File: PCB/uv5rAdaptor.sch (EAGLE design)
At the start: 2 parts

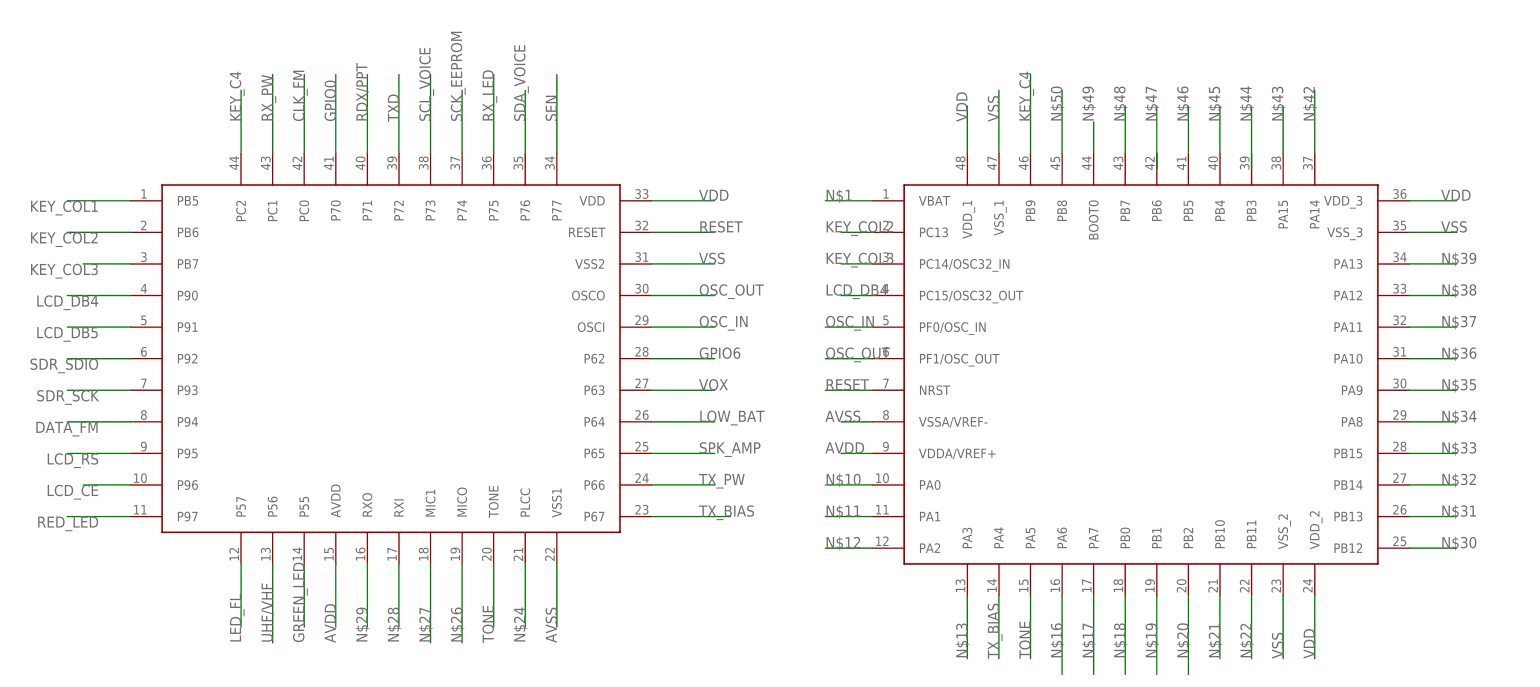
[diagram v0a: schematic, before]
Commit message: Link all points except for gpio6, we will do that once everything is routed
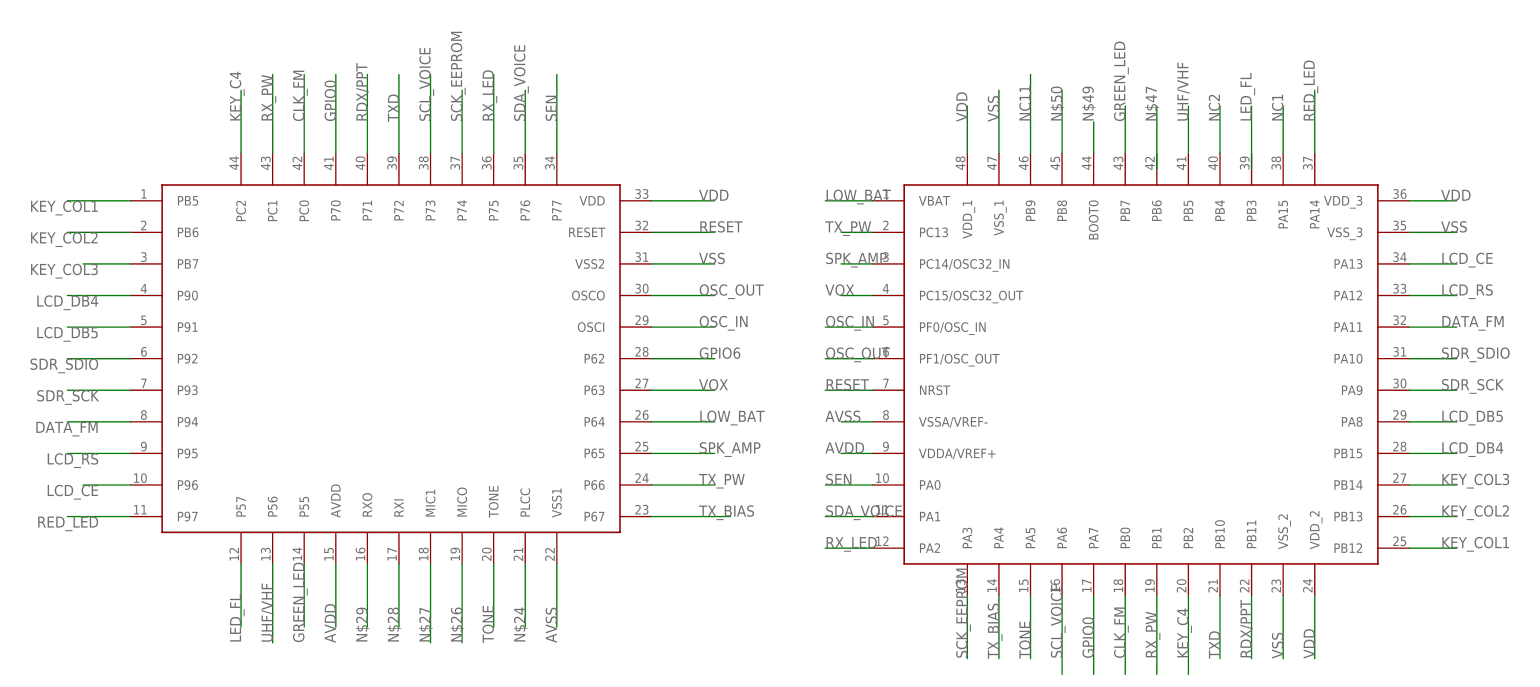
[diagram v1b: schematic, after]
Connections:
- net N$43 renamed NC1
- net N$45 renamed NC2
- removed net N$1: U$1.VBAT
- removed net N$10: U$1.PA0
- removed net N$11: U$1.PA1
- removed net N$12: U$1.PA2
- removed net N$13: U$1.PA3
- removed net N$16: U$1.PA6
- removed net N$17: U$1.PA7
- removed net N$18: U$1.PB0
- removed net N$19: U$1.PB1
- removed net N$20: U$1.PB2
- removed net N$21: U$1.PB10
- removed net N$22: U$1.PB11
- removed net N$30: U$1.PB12
- removed net N$31: U$1.PB13
- removed net N$32: U$1.PB14
- removed net N$33: U$1.PB15
- removed net N$34: U$1.PA8
- removed net N$35: U$1.PA9
- removed net N$36: U$1.PA10
- removed net N$37: U$1.PA11
- removed net N$38: U$1.PA12
- removed net N$39: U$1.PA13
- removed net N$42: U$1.PA14
- removed net N$46: U$1.PB5
- removed net N$48: U$1.PB7
- new net NC11: U$1.PB9
- net CLK_FM: now also U$1.PB0
- net DATA_FM: now also U$1.PA11
- net GPIO0: now also U$1.PA7
- net GREEN_LED: now also U$1.PB7
- net KEY_C4: now also U$1.PB2; no longer U$1.PB9
- net KEY_COL1: now also U$1.PB12
- net KEY_COL2: now also U$1.PB13; no longer U$1.PC13
- net KEY_COL3: now also U$1.PB14; no longer U$1.PC14/OSC32_IN
- net LCD_CE: now also U$1.PA13
- net LCD_DB4: now also U$1.PB15; no longer U$1.PC15/OSC32_OUT
- net LCD_DB5: now also U$1.PA8
- net LCD_RS: now also U$1.PA12
- net LOW_BAT: now also U$1.VBAT
- net RDX/PPT: now also U$1.PB11
- net RED_LED: now also U$1.PA14
- net RX_LED: now also U$1.PA2
- net RX_PW: now also U$1.PB1
- net SCK_EEPROM: now also U$1.PA3
- net SCL_VOICE: now also U$1.PA6
- net SDA_VOICE: now also U$1.PA1
- net SDR_SCK: now also U$1.PA9
- net SDR_SDIO: now also U$1.PA10
- net SEN: now also U$1.PA0
- net SPK_AMP: now also U$1.PC14/OSC32_IN
- net TXD: now also U$1.PB10
- net TX_PW: now also U$1.PC13
- net UHF/VHF: now also U$1.PB5
- net VOX: now also U$1.PC15/OSC32_OUT

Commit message: More routing
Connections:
- removed net N$50: U$1.PB8
- removed net NC1: U$1.PA15
- removed net NC11: U$1.PB9
- new net NC3: U$1.PC13
- new net NC4: U$1.PC14/OSC32_IN
- net LED_FL: now also U$1.PA15
- net SPK_AMP: now also U$1.PB9; no longer U$1.PC14/OSC32_IN
- net TX_PW: now also U$1.PB8; no longer U$1.PC13

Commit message: More traces
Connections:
- net KEY_C4: now also U$1.PB1; no longer U$1.PB2
- net RX_PW: now also U$1.PB2; no longer U$1.PB1
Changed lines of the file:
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@@
 </segment>
 <segment>
-<pinref part="U$1" gate="G$1" pin="PB2"/>
-<wire x1="142.24" y1="2.54" x2="142.24" y2="-10.16" width="0.1524" layer="91"/>
-<label x="142.24" y="-7.62" size="1.778" layer="95" rot="R90"/>
+<pinref part="U$1" gate="G$1" pin="PB1"/>
+<wire x1="137.16" y1="2.54" x2="137.16" y2="-10.16" width="0.1524" layer="91"/>
+<label x="137.16" y="-7.62" size="1.778" layer="95" rot="R90"/>
 </segment>
 </net>
@@
 </segment>
 <segment>
-<pinref part="U$1" gate="G$1" pin="PB1"/>
-<wire x1="137.16" y1="2.54" x2="137.16" y2="-10.16" width="0.1524" layer="91"/>
-<label x="137.16" y="-7.62" size="1.778" layer="95" rot="R90"/>
+<pinref part="U$1" gate="G$1" pin="PB2"/>
+<wire x1="142.24" y1="2.54" x2="142.24" y2="-10.16" width="0.1524" layer="91"/>
+<label x="142.24" y="-7.62" size="1.778" layer="95" rot="R90"/>
 </segment>
 </net>

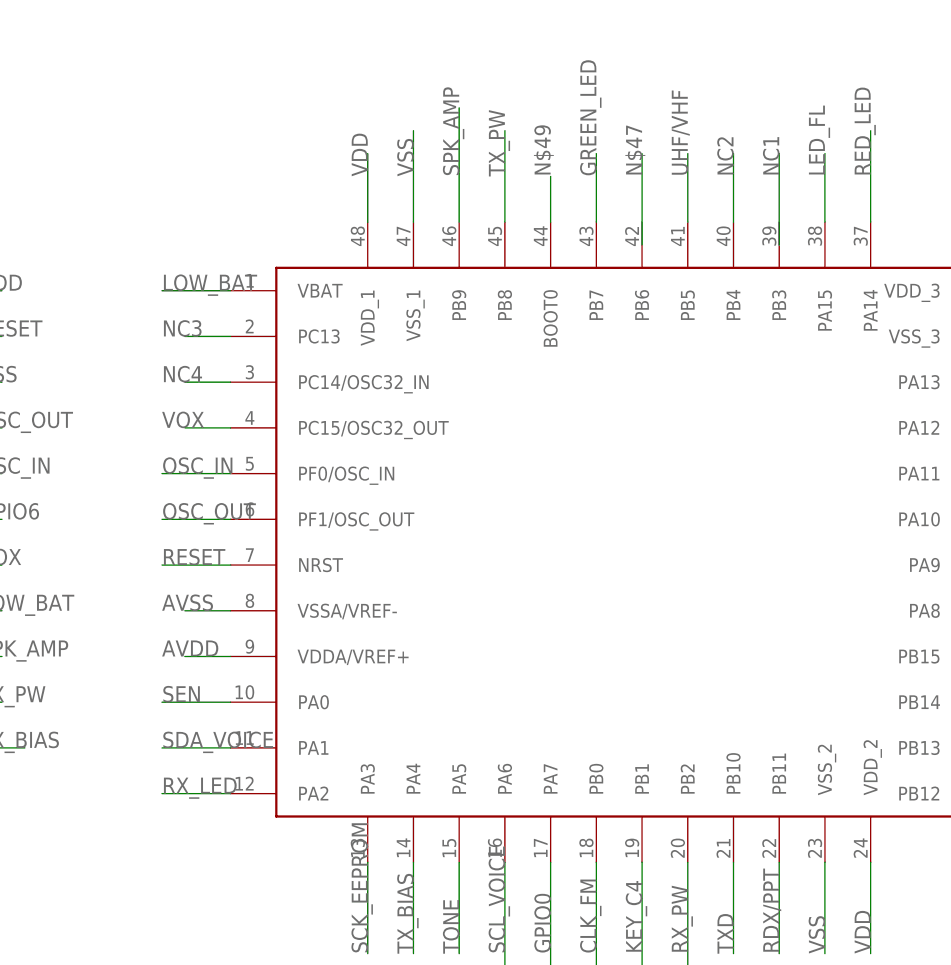
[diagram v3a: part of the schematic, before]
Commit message: Finished Routing
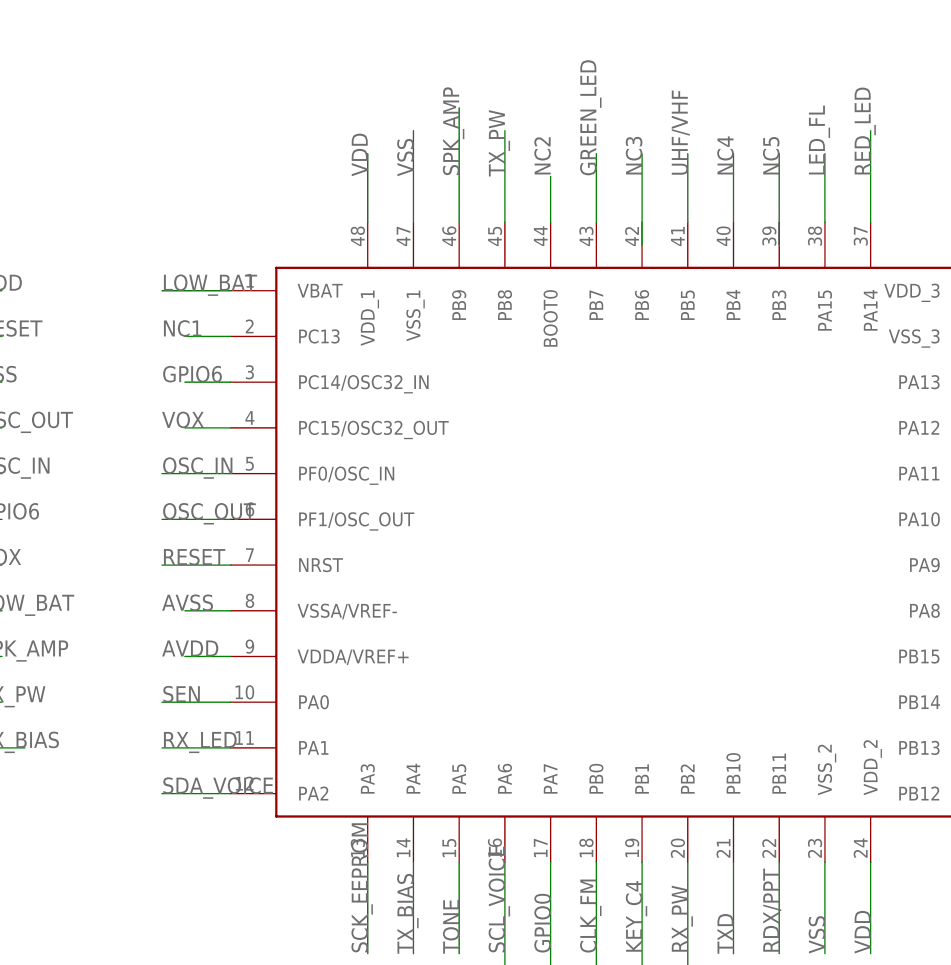
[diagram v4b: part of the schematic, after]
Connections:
- net NC3 renamed NC1
- removed net N$49: U$1.BOOT0
- net GPIO6: now also U$1.PC14/OSC32_IN
- net NC2: now also U$1.BOOT0; no longer U$1.PB4
- net NC4: now also U$1.PB4; no longer U$1.PC14/OSC32_IN
- net RX_LED: now also U$1.PA1; no longer U$1.PA2
- net SDA_VOICE: now also U$1.PA2; no longer U$1.PA1
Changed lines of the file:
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@@
+</segment>
+<segment>
+<pinref part="U$1" gate="G$1" pin="PA1"/>
+<wire x1="91.44" y1="15.24" x2="83.82" y2="15.24" width="0.1524" layer="91"/>
+<label x="83.82" y="15.24" size="1.778" layer="95"/>
+</segment>
+</net>
+<net name="SDA_VOICE" class="0">
+<segment>
+<wire x1="35.56" y1="73.66" x2="35.56" y2="83.82" width="0.1524" layer="91"/>
+<label x="35.56" y="78.74" size="1.778" layer="95" rot="R90"/>
+<pinref part="U$2" gate="G$1" pin="P76"/>
 </segment>
 <segment>
@@
 </segment>
 </net>
-<net name="SDA_VOICE" class="0">
-<segment>
-<wire x1="35.56" y1="73.66" x2="35.56" y2="83.82" width="0.1524" layer="91"/>
-<label x="35.56" y="78.74" size="1.778" layer="95" rot="R90"/>
-<pinref part="U$2" gate="G$1" pin="P76"/>
-</segment>
-<segment>
-<pinref part="U$1" gate="G$1" pin="PA1"/>
-<wire x1="91.44" y1="15.24" x2="83.82" y2="15.24" width="0.1524" layer="91"/>
-<label x="83.82" y="15.24" size="1.778" layer="95"/>
-</segment>
-</net>
 <net name="SEN" class="0">
 <segment>
@@
 <pinref part="U$2" gate="G$1" pin="P62"/>
 </segment>
+<segment>
+<pinref part="U$1" gate="G$1" pin="PC14/OSC32_IN"/>
+<wire x1="91.44" y1="55.88" x2="86.36" y2="55.88" width="0.1524" layer="91"/>
+<label x="83.82" y="55.88" size="1.778" layer="95"/>
+</segment>
 </net>
 <net name="VOX" class="0">
@@
 </segment>
 </net>
-<net name="N$47" class="0">
-<segment>
-<wire x1="137.16" y1="71.12" x2="137.16" y2="81.28" width="0.1524" layer="91"/>
-<label x="137.16" y="78.74" size="1.778" layer="95" rot="R90"/>
-</segment>
-</net>
-<net name="N$49" class="0">
+<net name="AVDD" class="0">
+<segment>
+<wire x1="5.08" y1="7.62" x2="5.08" y2="-2.54" width="0.1524" layer="91"/>
+<label x="5.08" y="-5.08" size="1.778" layer="95" rot="R90"/>
+<pinref part="U$2" gate="G$1" pin="AVDD"/>
+</segment>
+<segment>
+<pinref part="U$1" gate="G$1" pin="VDDA/VREF+"/>
+<wire x1="91.44" y1="25.4" x2="86.36" y2="25.4" width="0.1524" layer="91"/>
+<label x="83.82" y="25.4" size="1.778" layer="95"/>
+</segment>
+</net>
+<net name="AVSS" class="0">
+<segment>
+<wire x1="40.64" y1="7.62" x2="40.64" y2="-2.54" width="0.1524" layer="91"/>
+<label x="40.64" y="-5.08" size="1.778" layer="95" rot="R90"/>
+<pinref part="U$2" gate="G$1" pin="VSS1"/>
+</segment>
+<segment>
+<pinref part="U$1" gate="G$1" pin="VSSA/VREF-"/>
+<wire x1="91.44" y1="30.48" x2="86.36" y2="30.48" width="0.1524" layer="91"/>
+<label x="83.82" y="30.48" size="1.778" layer="95"/>
+</segment>
+</net>
+<net name="NC1" class="0">
+<segment>
+<pinref part="U$1" gate="G$1" pin="PC13"/>
+<wire x1="91.44" y1="60.96" x2="86.36" y2="60.96" width="0.1524" layer="91"/>
+<label x="83.82" y="60.96" size="1.778" layer="95"/>
+</segment>
+</net>
+<net name="NC2" class="0">
 <segment>
 <pinref part="U$1" gate="G$1" pin="BOOT0"/>
@@
 </segment>
 </net>
-<net name="AVDD" class="0">
-<segment>
-<wire x1="5.08" y1="7.62" x2="5.08" y2="-2.54" width="0.1524" layer="91"/>
-<label x="5.08" y="-5.08" size="1.778" layer="95" rot="R90"/>
-<pinref part="U$2" gate="G$1" pin="AVDD"/>
-</segment>
-<segment>
-<pinref part="U$1" gate="G$1" pin="VDDA/VREF+"/>
-<wire x1="91.44" y1="25.4" x2="86.36" y2="25.4" width="0.1524" layer="91"/>
-<label x="83.82" y="25.4" size="1.778" layer="95"/>
-</segment>
-</net>
-<net name="AVSS" class="0">
-<segment>
-<wire x1="40.64" y1="7.62" x2="40.64" y2="-2.54" width="0.1524" layer="91"/>
-<label x="40.64" y="-5.08" size="1.778" layer="95" rot="R90"/>
-<pinref part="U$2" gate="G$1" pin="VSS1"/>
-</segment>
-<segment>
-<pinref part="U$1" gate="G$1" pin="VSSA/VREF-"/>
-<wire x1="91.44" y1="30.48" x2="86.36" y2="30.48" width="0.1524" layer="91"/>
-<label x="83.82" y="30.48" size="1.778" layer="95"/>
-</segment>
-</net>
-<net name="NC2" class="0">
+<net name="NC3" class="0">
+<segment>
+<wire x1="137.16" y1="71.12" x2="137.16" y2="81.28" width="0.1524" layer="91"/>
+<label x="137.16" y="78.74" size="1.778" layer="95" rot="R90"/>
+</segment>
+</net>
+<net name="NC4" class="0">
 <segment>
 <pinref part="U$1" gate="G$1" pin="PB4"/>
@@
 </segment>
 </net>
-<net name="NC1" class="0">
+<net name="NC5" class="0">
 <segment>
 <wire x1="152.4" y1="71.12" x2="152.4" y2="81.28" width="0.1524" layer="91"/>
@@
 </segment>
 </net>
-<net name="NC4" class="0">
-<segment>
-<pinref part="U$1" gate="G$1" pin="PC14/OSC32_IN"/>
-<wire x1="91.44" y1="55.88" x2="86.36" y2="55.88" width="0.1524" layer="91"/>
-<label x="83.82" y="55.88" size="1.778" layer="95"/>
-</segment>
-</net>
-<net name="NC3" class="0">
-<segment>
-<pinref part="U$1" gate="G$1" pin="PC13"/>
-<wire x1="91.44" y1="60.96" x2="86.36" y2="60.96" width="0.1524" layer="91"/>
-<label x="83.82" y="60.96" size="1.778" layer="95"/>
-</segment>
-</net>

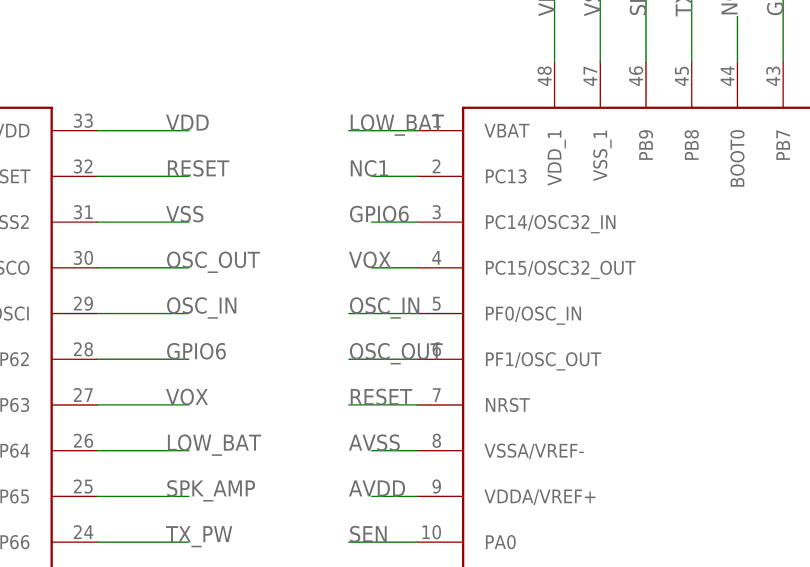
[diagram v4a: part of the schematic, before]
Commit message: Changed OSC pins to OSC32
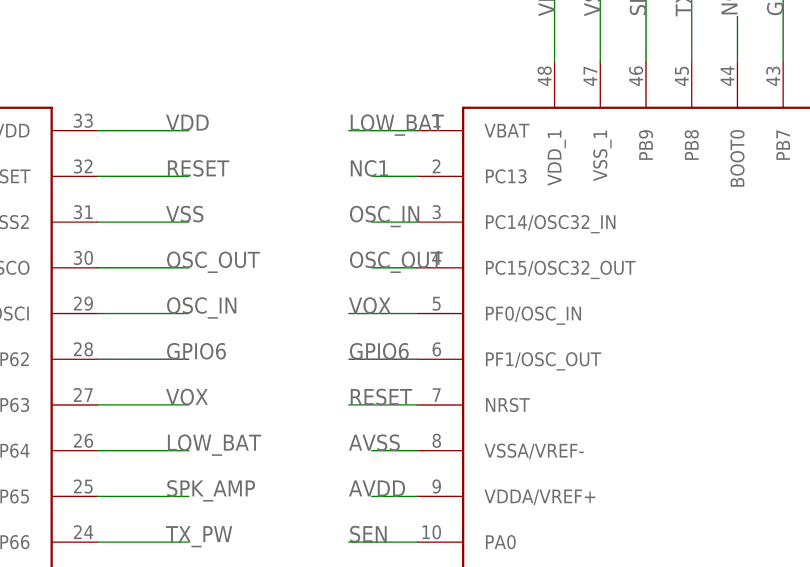
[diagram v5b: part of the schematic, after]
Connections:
- net GPIO6: now also U$1.PF1/OSC_OUT; no longer U$1.PC14/OSC32_IN
- net OSC_IN: now also U$1.PC14/OSC32_IN; no longer U$1.PF0/OSC_IN
- net OSC_OUT: now also U$1.PC15/OSC32_OUT; no longer U$1.PF1/OSC_OUT
- net VOX: now also U$1.PF0/OSC_IN; no longer U$1.PC15/OSC32_OUT
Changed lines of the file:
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@@
 </segment>
 <segment>
-<pinref part="U$1" gate="G$1" pin="PF1/OSC_OUT"/>
-<wire x1="91.44" y1="40.64" x2="83.82" y2="40.64" width="0.1524" layer="91"/>
-<label x="83.82" y="40.64" size="1.778" layer="95"/>
+<pinref part="U$1" gate="G$1" pin="PC15/OSC32_OUT"/>
+<wire x1="91.44" y1="50.8" x2="86.36" y2="50.8" width="0.1524" layer="91"/>
+<label x="83.82" y="50.8" size="1.778" layer="95"/>
 </segment>
 </net>
@@
 </segment>
 <segment>
-<pinref part="U$1" gate="G$1" pin="PF0/OSC_IN"/>
-<wire x1="91.44" y1="45.72" x2="83.82" y2="45.72" width="0.1524" layer="91"/>
-<label x="83.82" y="45.72" size="1.778" layer="95"/>
+<pinref part="U$1" gate="G$1" pin="PC14/OSC32_IN"/>
+<wire x1="91.44" y1="55.88" x2="86.36" y2="55.88" width="0.1524" layer="91"/>
+<label x="83.82" y="55.88" size="1.778" layer="95"/>
 </segment>
 </net>
@@
 </segment>
 <segment>
-<pinref part="U$1" gate="G$1" pin="PC14/OSC32_IN"/>
-<wire x1="91.44" y1="55.88" x2="86.36" y2="55.88" width="0.1524" layer="91"/>
-<label x="83.82" y="55.88" size="1.778" layer="95"/>
+<pinref part="U$1" gate="G$1" pin="PF1/OSC_OUT"/>
+<wire x1="91.44" y1="40.64" x2="83.82" y2="40.64" width="0.1524" layer="91"/>
+<label x="83.82" y="40.64" size="1.778" layer="95"/>
 </segment>
 </net>
@@
 </segment>
 <segment>
-<pinref part="U$1" gate="G$1" pin="PC15/OSC32_OUT"/>
-<wire x1="91.44" y1="50.8" x2="86.36" y2="50.8" width="0.1524" layer="91"/>
-<label x="83.82" y="50.8" size="1.778" layer="95"/>
+<pinref part="U$1" gate="G$1" pin="PF0/OSC_IN"/>
+<wire x1="91.44" y1="45.72" x2="83.82" y2="45.72" width="0.1524" layer="91"/>
+<label x="83.82" y="45.72" size="1.778" layer="95"/>
 </segment>
 </net>
